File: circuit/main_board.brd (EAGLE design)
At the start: 160 x 100 mm, 9 parts

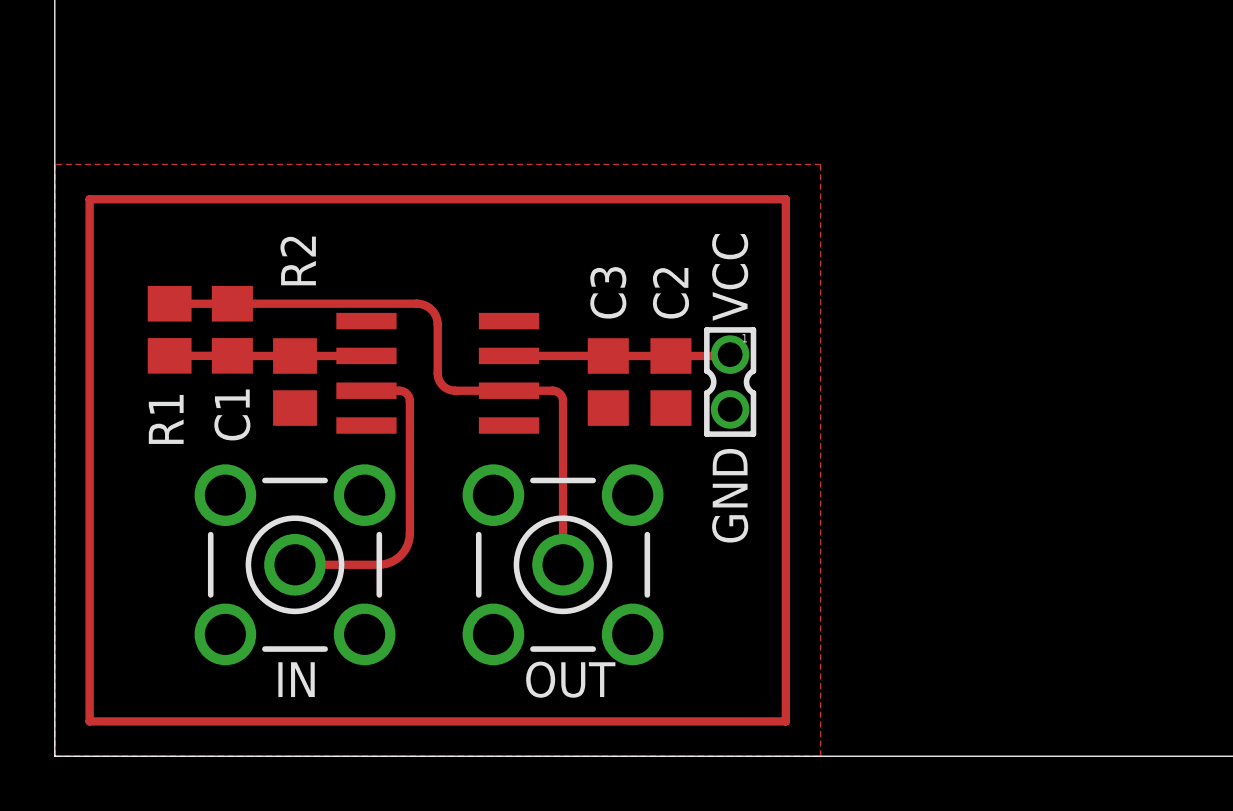
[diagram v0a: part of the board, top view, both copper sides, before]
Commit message: Added Schottky diode to Library; added Peak Detector to Schematic and Board
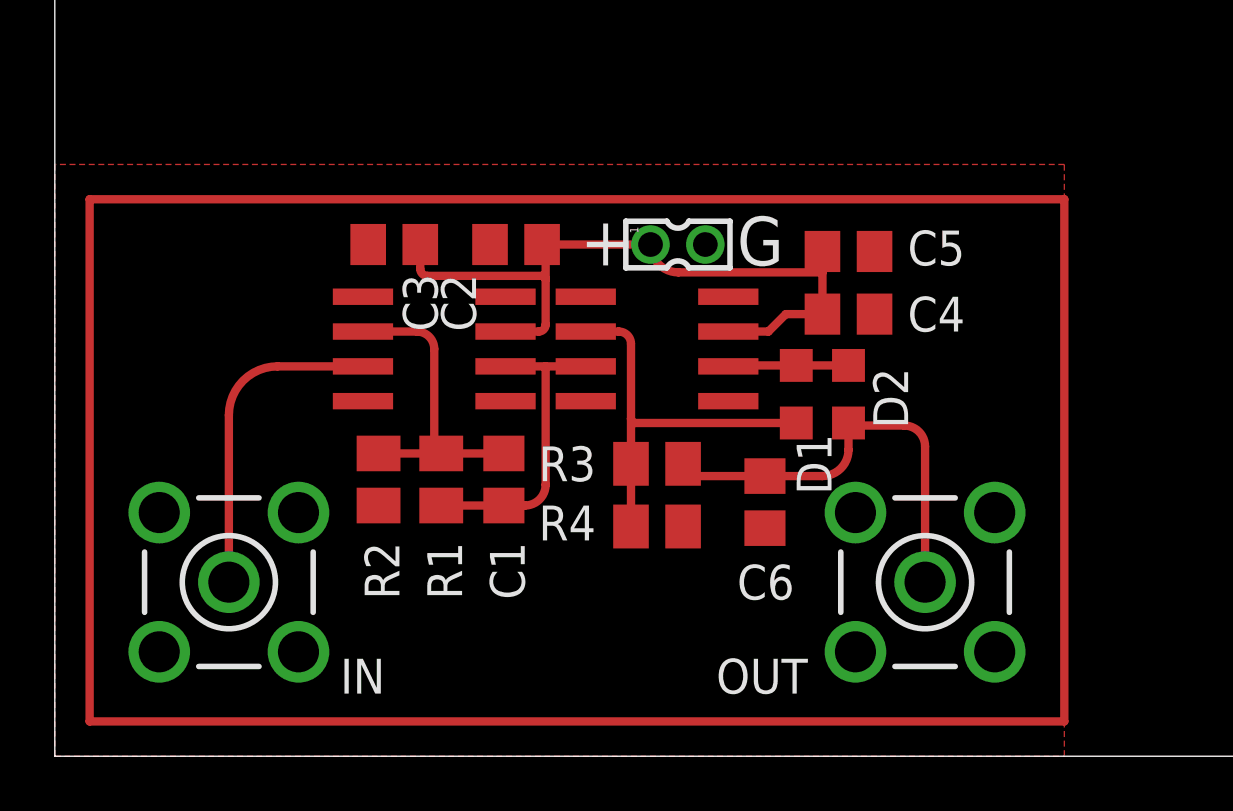
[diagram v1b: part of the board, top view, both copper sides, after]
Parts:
- added C4: 0.1uF, rcl:C0805
- added C5, C6: 10uF, rcl:C0805
- added D1, D2: (no value), 000phys605parts:SML0805
- added MAX4104_2: (no value), 000phys605parts:SO8
- added R3, R4: 100k, rcl:M0805
- C1: value (none) -> 5pF
- C2: value 10uF -> 0.1uF
- C3: value 0.1uF -> 10uF
- R1: value (none) -> 10k
- R2: value (none) -> 300
- moved OUT 13.2 mm to (31.8, 6.35), turned to 0 degrees
- moved C1 11.3 mm to (16.4, 10.1), turned to 90 degrees
- moved R1 11.3 mm to (14.1, 10.1), turned to 270 degrees
- moved C3 9.28 mm to (12.4, 18.7), turned to 180 degrees
- moved C2 7.56 mm to (16.8, 18.7), turned to 180 degrees
- moved SUP 5.37 mm to (22.7, 18.7), turned to 270 degrees
- moved R2 4.68 mm to (11.8, 10.1)
- moved IN 2.50 mm to (6.35, 6.35), turned to 180 degrees
- moved MAX4104_1 0.90 mm to (13.8, 14.9)
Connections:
- net IN- renamed IN-_1
- net VIN renamed IN
- removed net N$2: C2.1, C3.1, MAX4104_1.7, SUP.1
- removed net VOUT: C1.1, MAX4104_1.6, OUT.1, R1.2
- new net AMP: C1.1, MAX4104_1.6, MAX4104_2.3, R1.2
- new net DIG_READOUT: C6.1, D2.C, OUT.1, R3.2
- new net IN-_2: D1.A, MAX4104_2.2, R3.1, R4.1
- new net OUT_2: D1.C, D2.A, MAX4104_2.6
- new net VCC: C2.1, C3.1, C4.1, C5.1, MAX4104_1.7, MAX4104_2.7, SUP.1
- net GND: now also C4.2, C5.2, C6.2, MAX4104_2.4, R4.2
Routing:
- net VCC: track 0.00 -> 26.7 mm
- net VOUT: track 23.5 -> 0.00 mm
- net N$1: track 88.9 -> 109.2 mm
- net DIG_READOUT: track 0.00 -> 15.6 mm
- net IN-_2: track 0.00 -> 14.6 mm
- net AMP: track 0.00 -> 11.4 mm
- net N$2: track 8.09 -> 0.00 mm
- net OUT_2: track 0.00 -> 4.40 mm
- net IN-_1: track 7.19 -> 11.2 mm
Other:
- board text added: "+"
- board text added: "G"
- board text removed: "GND"
- board text removed: "VCC"
